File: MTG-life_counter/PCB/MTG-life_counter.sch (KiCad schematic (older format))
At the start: 28 parts, among them J1 USB_B_Mini, J2 AVR-ISP-6, U1 MCP73831-2-OT, U2 AT90S4433-8P, U3 HDSP-H101, U4 HDSP-H101, Y1 8 MHz

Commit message: Move the charger and battery stuff to a new sheet.
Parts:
- removed BT1: Battery_Cell, symbol Device:Battery_Cell
- removed C4, C5: C, symbol Device:C
- removed J1: USB_B_Mini, mibe:USB_Mini-B_Reichelt_BWM, symbol Connector:USB_B_Mini
- removed R1: R, symbol Device:R
- removed U1: MCP73831-2-OT, Package_TO_SOT_SMD:SOT-23-5, symbol Battery_Management:MCP73831-2-OT
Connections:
- net labels removed: +BATT, CHARGE_LED, SW_SPST
- wire segments 117 -> 90
- no-connect marks 7 -> 4
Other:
- note removed: "nominal\nvoltage:\n3.7 V"
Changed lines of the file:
@@
 $Descr A4 11693 8268
 encoding utf-8
-Sheet 1 1
+Sheet 1 2
 Title ""
 Date ""
@@
 Wire Wire Line
 	4100 2050 4400 2050
+$Sheet
+S 7150 4800 1350 900
+U 61835AF1
+F0 "Power" 50
+F1 "Power.sch" 50
+$EndSheet
+Wire Bus Line
+	5250 2600 5250 3750
 Wire Bus Line
 	8050 2600 8050 3650
 Wire Bus Line
 	9350 2600 9350 3650
-Wire Bus Line
-	5250 2600 5250 3750
-Text Notes 5400 6150 0    50   ~ 0
-nominal\nvoltage:\n3.7 V
-$Comp
-L Switch:SW_SPST #SW2
-U 1 1 6148AECB
-P 4900 5700
-F 0 "#SW2" H 4900 5935 50  0000 C CNN
-F 1 "SW_SPST" H 4900 5844 50  0000 C CNN
-F 2 "" H 4900 5700 50  0001 C CNN
-F 3 "~" H 4900 5700 50  0001 C CNN
-	1    4900 5700
-	1    0    0    -1
-$EndComp
-$Comp
-L power:VCC #PWR012
-U 1 1 6149EAE3
-P 5400 5650
-F 0 "#PWR012" H 5400 5500 50  0001 C CNN
-F 1 "VCC" H 5415 5823 50  0000 C CNN
-F 2 "" H 5400 5650 50  0001 C CNN
-F 3 "" H 5400 5650 50  0001 C CNN
-	1    5400 5650
-	1    0    0    -1
-$EndComp
-Wire Wire Line
-	5100 5700 5400 5700
-Wire Wire Line
-	5400 5700 5400 5650
-Wire Wire Line
-	1500 5400 1300 5400
-Wire Wire Line
-	1500 6000 1500 5400
-Wire Wire Line
-	1500 6400 1000 6400
-Connection ~ 1500 6400
-Wire Wire Line
-	1500 6300 1500 6400
-Wire Wire Line
-	3950 6400 4400 6400
-Connection ~ 3950 6400
-Wire Wire Line
-	3950 6200 3950 6400
-Wire Wire Line
-	3950 5900 3950 5700
-$Comp
-L Device:C C5
-U 1 1 614CCC8B
-P 3950 6050
-F 0 "C5" H 4065 6096 50  0000 L CNN
-F 1 "C" H 4065 6005 50  0000 L CNN
-F 2 "" H 3988 5900 50  0001 C CNN
-F 3 "~" H 3950 6050 50  0001 C CNN
-	1    3950 6050
-	1    0    0    -1
-$EndComp
-$Comp
-L Device:C C4
-U 1 1 614CBA2F
-P 1500 6150
-F 0 "C4" H 1615 6196 50  0000 L CNN
-F 1 "C" H 1615 6105 50  0000 L CNN
-F 2 "" H 1538 6000 50  0001 C CNN
-F 3 "~" H 1500 6150 50  0001 C CNN
-	1    1500 6150
-	1    0    0    -1
-$EndComp
-Wire Wire Line
-	3200 5900 3050 5900
-Text GLabel 3200 5900 2    50   Output ~ 0
-CHARGE_LED
-Wire Wire Line
-	4400 5700 4700 5700
-Wire Wire Line
-	3950 5700 4400 5700
-Connection ~ 4400 5700
-Wire Wire Line
-	4400 5700 4400 5650
-$Comp
-L power:+BATT #PWR09
-U 1 1 6149F617
-P 4400 5650
-F 0 "#PWR09" H 4400 5500 50  0001 C CNN
-F 1 "+BATT" H 4415 5823 50  0000 C CNN
-F 2 "" H 4400 5650 50  0001 C CNN
-F 3 "" H 4400 5650 50  0001 C CNN
-	1    4400 5650
-	1    0    0    -1
-$EndComp
-Wire Wire Line
-	2050 5900 2250 5900
-Wire Wire Line
-	2050 6000 2050 5900
-Wire Wire Line
-	2050 6400 1500 6400
-Connection ~ 2050 6400
-Wire Wire Line
-	2050 6300 2050 6400
-$Comp
-L Device:R R1
-U 1 1 6149905F
-P 2050 6150
-F 0 "R1" H 2120 6196 50  0000 L CNN
-F 1 "R" H 2120 6105 50  0000 L CNN
-F 2 "" V 1980 6150 50  0001 C CNN
-F 3 "~" H 2050 6150 50  0001 C CNN
-	1    2050 6150
-	1    0    0    -1
-$EndComp
-Wire Wire Line
-	4400 6400 4400 6200
-Wire Wire Line
-	1000 6400 1000 6450
-Connection ~ 1000 6400
-Wire Wire Line
-	1000 6000 1000 6400
-Wire Wire Line
-	4400 5700 4400 5900
-Connection ~ 3950 5700
-Wire Wire Line
-	3050 5700 3950 5700
-NoConn ~ 1300 5800
-NoConn ~ 1300 5700
-NoConn ~ 1300 5600
-Wire Wire Line
-	2650 6400 3950 6400
-Wire Wire Line
-	2650 6400 2050 6400
-Connection ~ 2650 6400
-Wire Wire Line
-	2650 6100 2650 6400
-Connection ~ 1500 5400
-Wire Wire Line
-	2650 5400 1500 5400
-Wire Wire Line
-	2650 5500 2650 5400
-$Comp
-L Battery_Management:MCP73831-2-OT U1
-U 1 1 6142838A
-P 2650 5800
-F 0 "U1" H 2750 6200 50  0000 L CNN
-F 1 "MCP73831-2-OT" H 2750 6100 50  0000 L CNN
-F 2 "Package_TO_SOT_SMD:SOT-23-5" H 2700 5550 50  0001 L CIN
-F 3 "http://ww1.microchip.com/downloads/en/DeviceDoc/20001984g.pdf" H 2500 5750 50  0001 C CNN
-	1    2650 5800
-	1    0    0    -1
-$EndComp
-$Comp
-L Connector:USB_B_Mini J1
-U 1 1 61439C57
-P 1000 5600
-F 0 "J1" H 1057 6067 50  0000 C CNN
-F 1 "USB_B_Mini" H 1057 5976 50  0000 C CNN
-F 2 "mibe:USB_Mini-B_Reichelt_BWM" H 1150 5550 50  0001 C CNN
-F 3 "~" H 1150 5550 50  0001 C CNN
-	1    1000 5600
-	1    0    0    -1
-$EndComp
-$Comp
-L power:GND #PWR01
-U 1 1 61439440
-P 1000 6450
-F 0 "#PWR01" H 1000 6200 50  0001 C CNN
-F 1 "GND" H 1005 6277 50  0000 C CNN
-F 2 "" H 1000 6450 50  0001 C CNN
-F 3 "" H 1000 6450 50  0001 C CNN
-	1    1000 6450
-	1    0    0    -1
-$EndComp
-$Comp
-L Device:Battery_Cell BT1
-U 1 1 6143801A
-P 4400 6100
-F 0 "BT1" H 4518 6196 50  0000 L CNN
-F 1 "Battery_Cell" H 4518 6105 50  0000 L CNN
-F 2 "" V 4400 6160 50  0001 C CNN
-F 3 "~" V 4400 6160 50  0001 C CNN
-	1    4400 6100
-	1    0    0    -1
-$EndComp
 $EndSCHEMATC

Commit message: Specify programming resistor and protection diode for charger.
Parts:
- C1: footprint (none) -> Capacitor_SMD:C_0805_2012Metric_Pad1.18x1.45mm_HandSolder
- R2: value R -> 130 Ω
- R3, R4, R5, R6, R7, R8: value 130 -> 130 Ω
- RV1: value 10 kOhm -> 10 kΩ
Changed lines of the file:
@@
 F 0 "C1" V 3598 1150 50  0000 C CNN
 F 1 "100 nF" V 3689 1150 50  0000 C CNN
-F 2 "" H 3888 1000 50  0001 C CNN
+F 2 "Capacitor_SMD:C_0805_2012Metric_Pad1.18x1.45mm_HandSolder" H 3888 1000 50  0001 C CNN
 F 3 "~" H 3850 1150 50  0001 C CNN
 	1    3850 1150
@@
 P 4400 3050
 F 0 "R2" V 4193 3050 50  0000 C CNN
-F 1 "R" V 4284 3050 50  0000 C CNN
+F 1 "130 Ω" V 4284 3050 50  0000 C CNN
 F 2 "Resistor_SMD:R_0805_2012Metric_Pad1.20x1.40mm_HandSolder" V 4330 3050 50  0001 C CNN
 F 3 "~" H 4400 3050 50  0001 C CNN
@@
 P 4400 3150
 F 0 "R3" V 4193 3150 50  0000 C CNN
-F 1 "130" V 4284 3150 50  0000 C CNN
+F 1 "130 Ω" V 4284 3150 50  0000 C CNN
 F 2 "Resistor_SMD:R_0805_2012Metric_Pad1.20x1.40mm_HandSolder" V 4330 3150 50  0001 C CNN
 F 3 "~" H 4400 3150 50  0001 C CNN
@@
 P 4400 3250
 F 0 "R4" V 4607 3250 50  0000 C CNN
-F 1 "130" V 4516 3250 50  0000 C CNN
+F 1 "130 Ω" V 4516 3250 50  0000 C CNN
 F 2 "Resistor_SMD:R_0805_2012Metric_Pad1.20x1.40mm_HandSolder" V 4330 3250 50  0001 C CNN
 F 3 "~" H 4400 3250 50  0001 C CNN
@@
 P 4400 3350
 F 0 "R5" V 4193 3350 50  0000 C CNN
-F 1 "130" V 4284 3350 50  0000 C CNN
+F 1 "130 Ω" V 4284 3350 50  0000 C CNN
 F 2 "Resistor_SMD:R_0805_2012Metric_Pad1.20x1.40mm_HandSolder" V 4330 3350 50  0001 C CNN
 F 3 "~" H 4400 3350 50  0001 C CNN
@@
 P 4400 3450
 F 0 "R6" V 4193 3450 50  0000 C CNN
-F 1 "130" V 4284 3450 50  0000 C CNN
+F 1 "130 Ω" V 4284 3450 50  0000 C CNN
 F 2 "Resistor_SMD:R_0805_2012Metric_Pad1.20x1.40mm_HandSolder" V 4330 3450 50  0001 C CNN
 F 3 "~" H 4400 3450 50  0001 C CNN
@@
 P 4400 3550
 F 0 "R7" V 4193 3550 50  0000 C CNN
-F 1 "130" V 4284 3550 50  0000 C CNN
+F 1 "130 Ω" V 4284 3550 50  0000 C CNN
 F 2 "Resistor_SMD:R_0805_2012Metric_Pad1.20x1.40mm_HandSolder" V 4330 3550 50  0001 C CNN
 F 3 "~" H 4400 3550 50  0001 C CNN
@@
 P 4400 3650
 F 0 "R8" V 4193 3650 50  0000 C CNN
-F 1 "130" V 4284 3650 50  0000 C CNN
+F 1 "130 Ω" V 4284 3650 50  0000 C CNN
 F 2 "Resistor_SMD:R_0805_2012Metric_Pad1.20x1.40mm_HandSolder" V 4330 3650 50  0001 C CNN
 F 3 "~" H 4400 3650 50  0001 C CNN
@@
 P 4750 2450
 F 0 "RV1" H 4680 2404 50  0000 R CNN
-F 1 "10 kOhm" H 4680 2495 50  0000 R CNN
+F 1 "10 kΩ" H 4680 2495 50  0000 R CNN
 F 2 "" H 4750 2450 50  0001 C CNN
 F 3 "~" H 4750 2450 50  0001 C CNN
@@
 F0 "Power" 50
 F1 "Power.sch" 50
+F2 "VUSB" O L 7150 5100 50
 $EndSheet
 Wire Bus Line

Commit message: Add a voltage monitor to be used to reset the microcontroller.
This is used as sort of a undervoltage lockout protection to protect the battery. The threshold voltage of the used IC is 3.08 V, which is near the minimum discharge voltage of a LiPo battery of 3 V.
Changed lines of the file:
@@
 F1 "Power.sch" 50
 F2 "VUSB" O L 7150 5100 50
+F3 "~BATT_LOW" O R 8500 5100 50
 $EndSheet
 Wire Bus Line

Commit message: Power schematic is pretty much done.
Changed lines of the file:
@@
 F0 "Power" 50
 F1 "Power.sch" 50
-F2 "VUSB" O L 7150 5100 50
-F3 "~BATT_LOW" O R 8500 5100 50
+F2 "~BATT_LOW" O R 8500 5100 50
+F3 "VUSB" O L 7150 5100 50
+F4 "CHARGER_STAT" O L 7150 5400 50
 $EndSheet
 Wire Bus Line

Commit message: Reset circuitry
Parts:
- added Q1: IRLML6244, symbol Device:Q_NMOS_GSD
- added R11: 10 kΩ, Resistor_SMD:R_0805_2012Metric_Pad1.20x1.40mm_HandSolder, symbol Device:R
- added R12: 100 kΩ, Resistor_SMD:R_0805_2012Metric_Pad1.20x1.40mm_HandSolder, symbol Device:R
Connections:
- wire segments 90 -> 101
- no-connect marks 4 -> 5
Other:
- moved on the sheet: H1, H2, H3, H4
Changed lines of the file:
@@
 L Mechanical:MountingHole_Pad H1
 U 1 1 614BC040
-P 1000 7350
-F 0 "H1" H 1100 7399 50  0000 L CNN
-F 1 "MountingHole_Pad" H 1100 7308 50  0000 L CNN
-F 2 "MountingHole:MountingHole_3.2mm_M3_Pad_Via" H 1000 7350 50  0001 C CNN
-F 3 "~" H 1000 7350 50  0001 C CNN
-	1    1000 7350
+P 7250 6100
+F 0 "H1" H 7350 6149 50  0000 L CNN
+F 1 "MountingHole_Pad" H 7350 6058 50  0000 L CNN
+F 2 "MountingHole:MountingHole_3.2mm_M3_Pad_Via" H 7250 6100 50  0001 C CNN
+F 3 "~" H 7250 6100 50  0001 C CNN
+	1    7250 6100
 	1    0    0    -1
 $EndComp
@@
 L Mechanical:MountingHole_Pad H2
 U 1 1 614BCA90
-P 1950 7350
-F 0 "H2" H 2050 7399 50  0000 L CNN
-F 1 "MountingHole_Pad" H 2050 7308 50  0000 L CNN
-F 2 "MountingHole:MountingHole_3.2mm_M3_Pad_Via" H 1950 7350 50  0001 C CNN
-F 3 "~" H 1950 7350 50  0001 C CNN
-	1    1950 7350
+P 8200 6100
+F 0 "H2" H 8300 6149 50  0000 L CNN
+F 1 "MountingHole_Pad" H 8300 6058 50  0000 L CNN
+F 2 "MountingHole:MountingHole_3.2mm_M3_Pad_Via" H 8200 6100 50  0001 C CNN
+F 3 "~" H 8200 6100 50  0001 C CNN
+	1    8200 6100
 	1    0    0    -1
 $EndComp
@@
 L Mechanical:MountingHole_Pad H3
 U 1 1 614BD66E
-P 2900 7350
-F 0 "H3" H 3000 7399 50  0000 L CNN
-F 1 "MountingHole_Pad" H 3000 7308 50  0000 L CNN
-F 2 "MountingHole:MountingHole_3.2mm_M3_Pad_Via" H 2900 7350 50  0001 C CNN
-F 3 "~" H 2900 7350 50  0001 C CNN
-	1    2900 7350
+P 9150 6100
+F 0 "H3" H 9250 6149 50  0000 L CNN
+F 1 "MountingHole_Pad" H 9250 6058 50  0000 L CNN
+F 2 "MountingHole:MountingHole_3.2mm_M3_Pad_Via" H 9150 6100 50  0001 C CNN
+F 3 "~" H 9150 6100 50  0001 C CNN
+	1    9150 6100
 	1    0    0    -1
 $EndComp
@@
 L Mechanical:MountingHole_Pad H4
 U 1 1 614BDC32
-P 3850 7350
-F 0 "H4" H 3950 7399 50  0000 L CNN
-F 1 "MountingHole_Pad" H 3950 7308 50  0000 L CNN
-F 2 "MountingHole:MountingHole_3.2mm_M3_Pad_Via" H 3850 7350 50  0001 C CNN
-F 3 "~" H 3850 7350 50  0001 C CNN
-	1    3850 7350
+P 10100 6100
+F 0 "H4" H 10200 6149 50  0000 L CNN
+F 1 "MountingHole_Pad" H 10200 6058 50  0000 L CNN
+F 2 "MountingHole:MountingHole_3.2mm_M3_Pad_Via" H 10100 6100 50  0001 C CNN
+F 3 "~" H 10100 6100 50  0001 C CNN
+	1    10100 6100
 	1    0    0    -1
 $EndComp
@@
 L power:GND #PWR02
 U 1 1 614BE552
-P 1000 7550
-F 0 "#PWR02" H 1000 7300 50  0001 C CNN
-F 1 "GND" H 1005 7377 50  0000 C CNN
-F 2 "" H 1000 7550 50  0001 C CNN
-F 3 "" H 1000 7550 50  0001 C CNN
-	1    1000 7550
-	1    0    0    -1
-$EndComp
-Wire Wire Line
-	1000 7550 1000 7500
-Wire Wire Line
-	1000 7500 1950 7500
-Wire Wire Line
-	1950 7500 1950 7450
-Connection ~ 1000 7500
-Wire Wire Line
-	1000 7500 1000 7450
-Wire Wire Line
-	1950 7500 2900 7500
-Wire Wire Line
-	2900 7500 2900 7450
-Connection ~ 1950 7500
-Wire Wire Line
-	2900 7500 3850 7500
-Wire Wire Line
-	3850 7500 3850 7450
-Connection ~ 2900 7500
+P 7250 6300
+F 0 "#PWR02" H 7250 6050 50  0001 C CNN
+F 1 "GND" H 7255 6127 50  0000 C CNN
+F 2 "" H 7250 6300 50  0001 C CNN
+F 3 "" H 7250 6300 50  0001 C CNN
+	1    7250 6300
+	1    0    0    -1
+$EndComp
+Wire Wire Line
+	7250 6300 7250 6250
+Wire Wire Line
+	7250 6250 8200 6250
+Wire Wire Line
+	8200 6250 8200 6200
+Connection ~ 7250 6250
+Wire Wire Line
+	7250 6250 7250 6200
+Wire Wire Line
+	8200 6250 9150 6250
+Wire Wire Line
+	9150 6250 9150 6200
+Connection ~ 8200 6250
+Wire Wire Line
+	9150 6250 10100 6250
+Wire Wire Line
+	10100 6250 10100 6200
+Connection ~ 9150 6250
 Text Label 4300 1750 0    50   ~ 0
 SW_DEC
@@
 	4100 2050 4400 2050
 $Sheet
-S 7150 4800 1350 900
+S 850  5700 1350 900
 U 61835AF1
 F0 "Power" 50
 F1 "Power.sch" 50
-F2 "~BATT_LOW" O R 8500 5100 50
-F3 "VUSB" O L 7150 5100 50
-F4 "CHARGER_STAT" O L 7150 5400 50
+F2 "~BATT_LOW" O R 2200 5800 50
+F3 "VUSB" O R 2200 6100 50
+F4 "CHARGER_STAT" O R 2200 6400 50
 $EndSheet
-Wire Bus Line
-	5250 2600 5250 3750
+$Comp
+L power:GND #PWR012
+U 1 1 619FDBF8
+P 4100 6400
+F 0 "#PWR012" H 4100 6150 50  0001 C CNN
+F 1 "GND" H 4105 6227 50  0000 C CNN
+F 2 "" H 4100 6400 50  0001 C CNN
+F 3 "" H 4100 6400 50  0001 C CNN
+	1    4100 6400
+	1    0    0    -1
+$EndComp
+Wire Wire Line
+	4100 6400 4100 6350
+Text GLabel 4650 5800 2    50   Output ~ 0
+~RESET
+Wire Wire Line
+	4650 5800 4100 5800
+Wire Wire Line
+	4100 5800 4100 5900
+Wire Wire Line
+	2200 6100 3300 6100
+$Comp
+L Device:R R12
+U 1 1 61A098B5
+P 3600 6350
+F 0 "R12" V 3393 6350 50  0000 C CNN
+F 1 "100 kΩ" V 3484 6350 50  0000 C CNN
+F 2 "Resistor_SMD:R_0805_2012Metric_Pad1.20x1.40mm_HandSolder" V 3530 6350 50  0001 C CNN
+F 3 "~" H 3600 6350 50  0001 C CNN
+	1    3600 6350
+	0    1    1    0
+$EndComp
+Wire Wire Line
+	3450 6350 3300 6350
+Wire Wire Line
+	3300 6350 3300 6100
+Connection ~ 3300 6100
+Wire Wire Line
+	3300 6100 3800 6100
+Wire Wire Line
+	3750 6350 4100 6350
+Connection ~ 4100 6350
+Wire Wire Line
+	4100 6350 4100 6300
+Wire Wire Line
+	2200 5800 3450 5800
+Connection ~ 4100 5800
+$Comp
+L Device:R R11
+U 1 1 61A174B7
+P 3600 5800
+F 0 "R11" V 3393 5800 50  0000 C CNN
+F 1 "10 kΩ" V 3484 5800 50  0000 C CNN
+F 2 "Resistor_SMD:R_0805_2012Metric_Pad1.20x1.40mm_HandSolder" V 3530 5800 50  0001 C CNN
+F 3 "~" H 3600 5800 50  0001 C CNN
+	1    3600 5800
+	0    1    1    0
+$EndComp
+Wire Wire Line
+	3750 5800 4100 5800
+NoConn ~ 8400 3750
 Wire Bus Line
 	8050 2600 8050 3650
 Wire Bus Line
 	9350 2600 9350 3650
+Wire Bus Line
+	5250 2600 5250 3750
+$Comp
+L Device:Q_NMOS_GSD Q1
+U 1 1 619F4049
+P 4000 6100
+F 0 "Q1" H 4204 6146 50  0000 L CNN
+F 1 "IRLML6244" H 4204 6055 50  0000 L CNN
+F 2 "" H 4200 6200 50  0001 C CNN
+F 3 "~" H 4000 6100 50  0001 C CNN
+	1    4000 6100
+	1    0    0    -1
+$EndComp
 $EndSCHEMATC

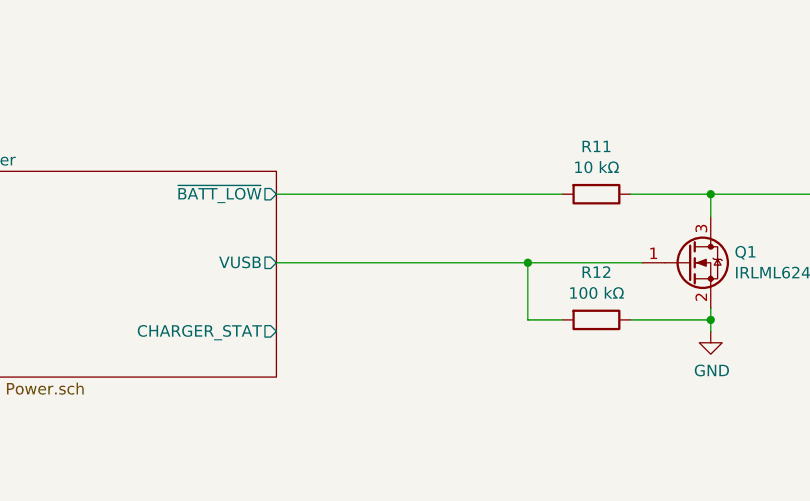
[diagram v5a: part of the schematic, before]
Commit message: Add charging LED.
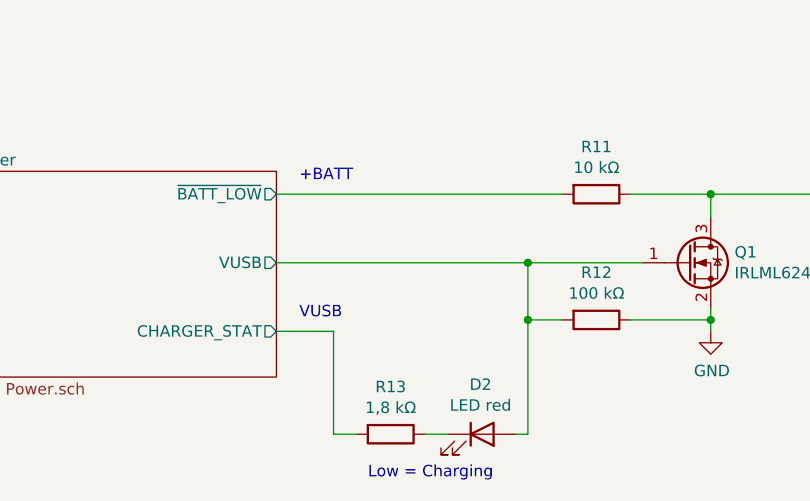
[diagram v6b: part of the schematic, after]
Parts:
- added D2: LED red, LED_THT:LED_D3.0mm, symbol Device:LED
- added R13: 1,8 kΩ, Resistor_SMD:R_0805_2012Metric_Pad1.20x1.40mm_HandSolder, symbol Device:R
- Q1: footprint (none) -> Package_TO_SOT_SMD:SOT-23_Handsoldering
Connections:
- wire segments 101 -> 107
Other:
- note added: "+BATT"
- note added: "Low = Charging"
- note added: "VUSB"
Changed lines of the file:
@@
 	3750 5800 4100 5800
 NoConn ~ 8400 3750
+$Comp
+L Device:Q_NMOS_GSD Q1
+U 1 1 619F4049
+P 4000 6100
+F 0 "Q1" H 4204 6146 50  0000 L CNN
+F 1 "IRLML6244" H 4204 6055 50  0000 L CNN
+F 2 "Package_TO_SOT_SMD:SOT-23_Handsoldering" H 4200 6200 50  0001 C CNN
+F 3 "~" H 4000 6100 50  0001 C CNN
+	1    4000 6100
+	1    0    0    -1
+$EndComp
+Text Notes 2300 5750 0    50   ~ 0
++BATT
+$Comp
+L Device:LED D2
+U 1 1 61A3EFBD
+P 3100 6850
+F 0 "D2" H 3093 7067 50  0000 C CNN
+F 1 "LED red" H 3093 6976 50  0000 C CNN
+F 2 "LED_THT:LED_D3.0mm" H 3100 6850 50  0001 C CNN
+F 3 "~" H 3100 6850 50  0001 C CNN
+F 4 "Vf 1.6 V; If 2 mA" H 3100 6850 50  0001 C CNN "Characteristics"
+	1    3100 6850
+	1    0    0    -1
+$EndComp
+$Comp
+L Device:R R13
+U 1 1 61A40252
+P 2700 6850
+F 0 "R13" V 2493 6850 50  0000 C CNN
+F 1 "1,8 kΩ" V 2584 6850 50  0000 C CNN
+F 2 "Resistor_SMD:R_0805_2012Metric_Pad1.20x1.40mm_HandSolder" V 2630 6850 50  0001 C CNN
+F 3 "~" H 2700 6850 50  0001 C CNN
+	1    2700 6850
+	0    1    1    0
+$EndComp
+Wire Wire Line
+	3250 6850 3300 6850
+Wire Wire Line
+	3300 6850 3300 6350
+Connection ~ 3300 6350
+Wire Wire Line
+	2950 6850 2850 6850
+Wire Wire Line
+	2550 6850 2450 6850
+Wire Wire Line
+	2450 6850 2450 6400
+Wire Wire Line
+	2450 6400 2200 6400
 Wire Bus Line
 	8050 2600 8050 3650
@@
 Wire Bus Line
 	5250 2600 5250 3750
-$Comp
-L Device:Q_NMOS_GSD Q1
-U 1 1 619F4049
-P 4000 6100
-F 0 "Q1" H 4204 6146 50  0000 L CNN
-F 1 "IRLML6244" H 4204 6055 50  0000 L CNN
-F 2 "" H 4200 6200 50  0001 C CNN
-F 3 "~" H 4000 6100 50  0001 C CNN
-	1    4000 6100
-	1    0    0    -1
-$EndComp
+Text Notes 2300 6350 0    50   ~ 0
+VUSB
+Text Notes 2600 7050 0    50   ~ 0
+Low = Charging
 $EndSCHEMATC

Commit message: Add digit multiplexing.
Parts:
- added Q2: IRLML6244, Package_TO_SOT_SMD:SOT-23_Handsoldering, symbol Device:Q_NMOS_GSD
- added Q4, Q5: Si2301DS, Package_TO_SOT_SMD:SOT-23_Handsoldering, symbol Device:Q_PMOS_GSD
- added R14: 180 Ω, Resistor_SMD:R_0805_2012Metric_Pad1.20x1.40mm_HandSolder, symbol Device:R
- added R15: 10 kΩ, Resistor_SMD:R_0805_2012Metric_Pad1.20x1.40mm_HandSolder, symbol Device:R
- added R16: 150 Ω, Resistor_SMD:R_0805_2012Metric_Pad1.20x1.40mm_HandSolder, symbol Device:R
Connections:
- net labels added: +BATT, DIGIT_MULTIPLEXER
- net labels removed: VCC
- wire segments 107 -> 136
- no-connect marks 5 -> 7
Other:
- moved on the sheet: J2, R9, U4

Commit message: The 7-seg. displays are now using the correct footprint.
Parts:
- U3, U4: footprint Display_7Segment:HDSP-A401 -> mibe:HDSP-H101
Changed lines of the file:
@@
 F 0 "U3" H 8700 4017 50  0000 C CNN
 F 1 "HDSP-H101" H 8700 3926 50  0000 C CNN
-F 2 "Display_7Segment:HDSP-A401" H 8700 2800 50  0001 C CNN
+F 2 "mibe:HDSP-H101" H 8700 2800 50  0001 C CNN
 F 3 "https://docs.broadcom.com/docs/AV02-2553EN" H 7900 4350 50  0001 C CNN
 	1    8700 3350
@@
 F 0 "U4" H 10300 4017 50  0000 C CNN
 F 1 "HDSP-H101" H 10300 3926 50  0000 C CNN
-F 2 "Display_7Segment:HDSP-A401" H 10300 2800 50  0001 C CNN
+F 2 "mibe:HDSP-H101" H 10300 2800 50  0001 C CNN
 F 3 "https://docs.broadcom.com/docs/AV02-2553EN" H 9500 4350 50  0001 C CNN
 	1    10300 3350
